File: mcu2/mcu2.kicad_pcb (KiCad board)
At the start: 2 copper layers, 96.7 x 58.3 mm, 36 parts, among them J1 KF128-5.08, J2 Conn_01x30, J8 Conn_01x30, Q1 WSF3085, Q2 PL4009, Q3 PL4009, U1 Pico, U2 motor_driver, U3 max31865_module, U4 dcdc_module

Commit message: mcu2 gerber
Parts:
- moved REF** 0.60 mm to (178.4, 141.5)
- moved REF** 0.51 mm to (178.3, 90.9)
- moved REF** 0.50 mm to (88.6, 141.5)
- moved REF** 0.44 mm to (88.6, 90.9)
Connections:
- J2 pad 6: GNDA -> THERM_AUX_2
- J2 pad 7: THERM_0 -> THERM_AUX_1
- J2 pad 8: THERM_AUX_1 -> THERM_0
- J2 pad 9: THERM_AUX_2 -> GNDA
- J8 pad 6: GNDA -> THERM_AUX_2
- J8 pad 7: THERM_0 -> THERM_AUX_1
- J8 pad 8: THERM_AUX_1 -> THERM_0
- J8 pad 9: THERM_AUX_2 -> GNDA
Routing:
- net +5V: track 28.0 -> 38.5 mm
- net GNDA: track 40.5 -> 33.0 mm, vias 0 -> 27
- net PROBE_ZMIN_24V: track 43.7 -> 37.7 mm
- net THERM_AUX_2: track 118.1 -> 112.7 mm, vias 2 -> 0
- net PART_FAN_CTRL: track 19.2 -> 13.9 mm
- net ADXL345_CS: track 49.6 -> 45.7 mm
- net ADXL345_SDO: track 53.4 -> 49.7 mm
- net SERVO_NEOPIXEL: track 61.9 -> 58.3 mm
- net GND: track 26.4 -> 29.5 mm, vias 19 -> 90
- net AUX2: track 28.6 -> 25.5 mm
- net E_DIR: track 42.5 -> 39.7 mm
- net STEPPER_A2: track 23.9 -> 21.6 mm
- net ADXL345_SDA: track 50.8 -> 48.7 mm
- net HEATER_CTRL: track 30.9 -> 28.9 mm
- net E_CS: track 45.4 -> 43.6 mm
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- added copper zone on B.Cu, net GND
- added copper zone on F.Cu, net GND
- added copper zone on F.Cu, net GNDA
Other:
- board size 96.7 x 58.3 mm -> 96.8 x 57.7 mm
- board text removed: "24V"
- board text removed: "3V3"
- board text removed: "CS"
- board text removed: "DIR"
- board text removed: "EN"
- board text removed: "G"
- board text removed: "GND"
- board text removed: "STEP"
- board text removed: "STEPPER"

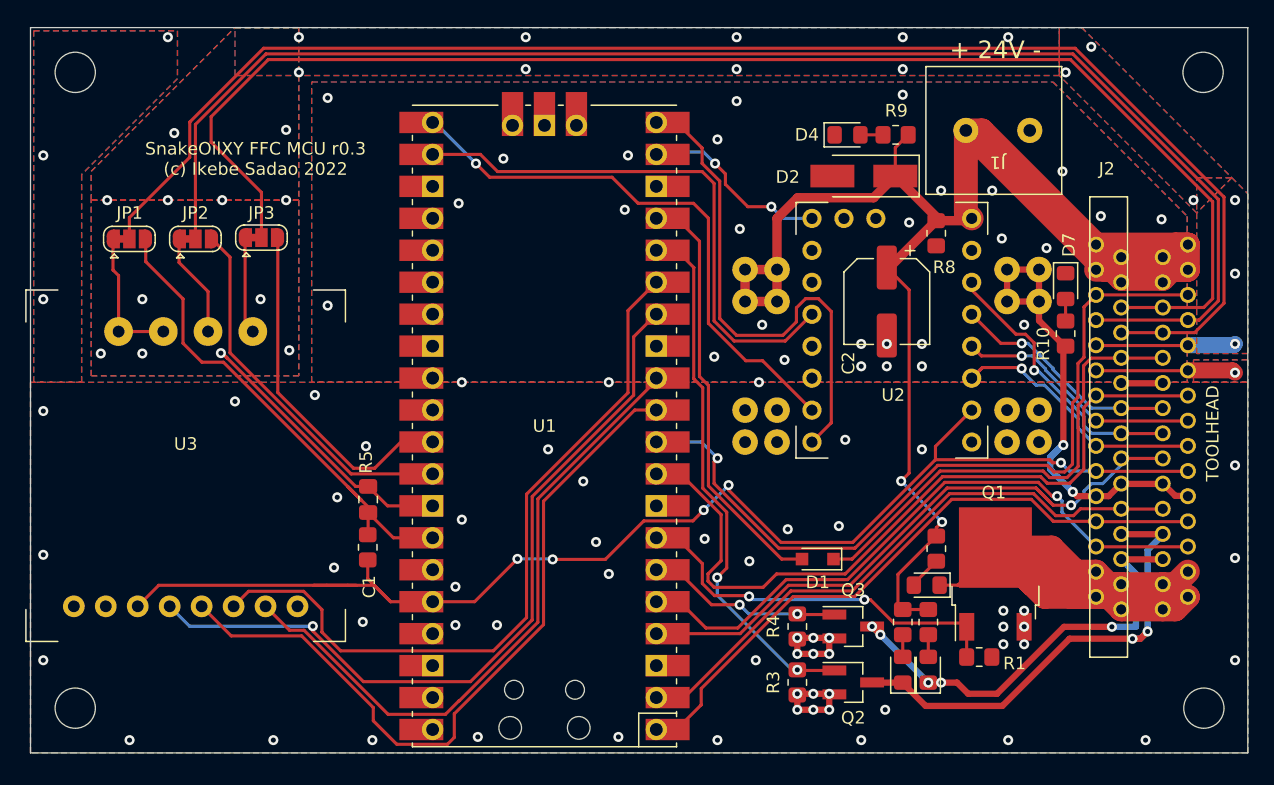
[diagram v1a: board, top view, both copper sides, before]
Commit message: change hole size
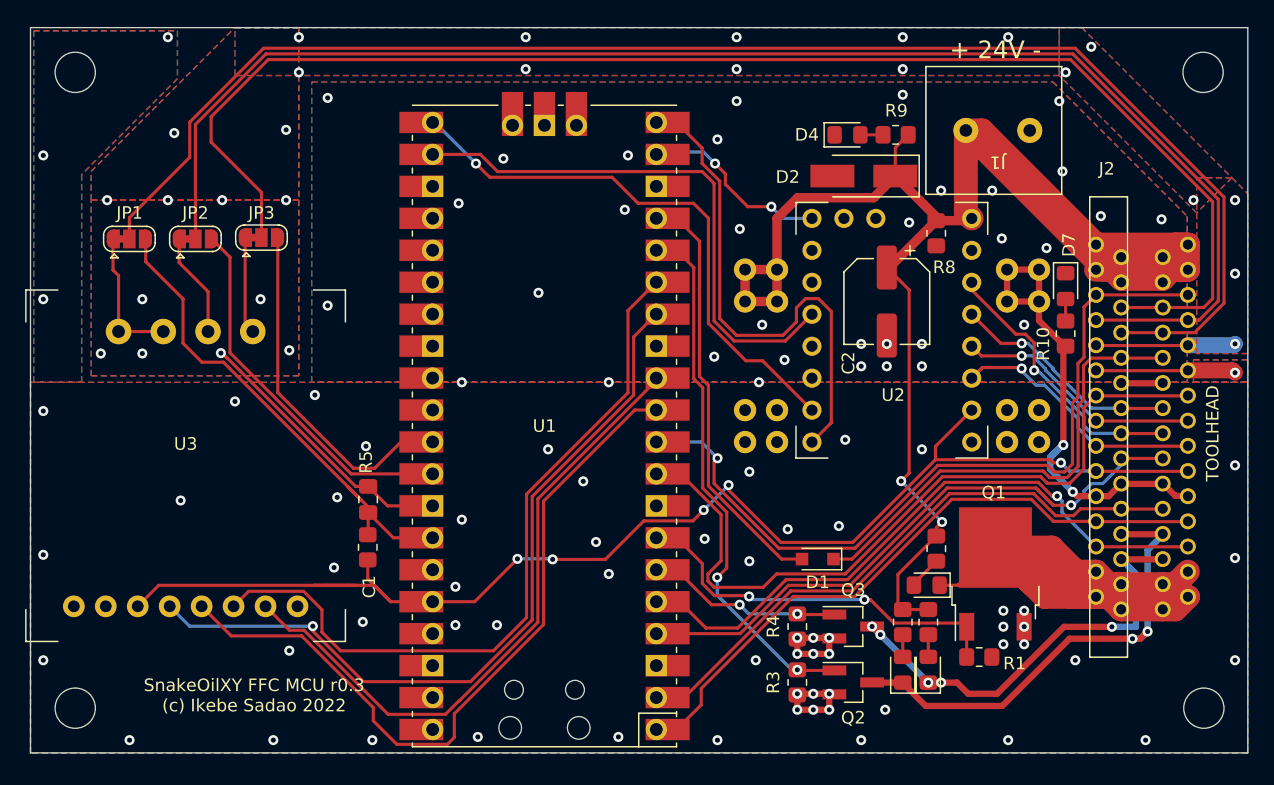
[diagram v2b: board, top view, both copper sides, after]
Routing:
- net GND: vias 90 -> 96

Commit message: r3 jlcpcb
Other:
- outline, holes or cut-outs redrawn
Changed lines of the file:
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@@
       (net 4 "HEATER_SW") (pinfunction "Pin_30") (pintype "passive"))
   )
-  (gr_rect (start 181.864 87.376) (end 85.09 145.034) (layer "Edge.Cuts") (width 0.1) (fill none))
+  (gr_line (start 180.594 145.034) (end 86.36 145.034) (layer "Edge.Cuts") (width 0.1))
+  (gr_line (start 85.09 143.764) (end 85.09 88.646) (layer "Edge.Cuts") (width 0.1))
+  (gr_arc (start 181.864 143.764) (mid 181.492026 144.662026) (end 180.594 145.034) (layer "Edge.Cuts") (width 0.1))
+  (gr_line (start 181.864 88.646) (end 181.864 143.764) (layer "Edge.Cuts") (width 0.1))
+  (gr_arc (start 86.36 145.034) (mid 85.461974 144.662026) (end 85.09 143.764) (layer "Edge.Cuts") (width 0.1))
+  (gr_arc (start 180.594 87.376) (mid 181.492026 87.747974) (end 181.864 88.646) (layer "Edge.Cuts") (width 0.1))
+  (gr_line (start 86.36 87.376) (end 180.594 87.376) (layer "Edge.Cuts") (width 0.1))
+  (gr_arc (start 85.09 88.646) (mid 85.461974 87.747974) (end 86.36 87.376) (layer "Edge.Cuts") (width 0.1))
   (gr_text "SnakeOilXY FFC MCU r0.3\n(c) Ikebe Sadao 2022" (at 102.87 140.462) (layer "F.SilkS")
     (effects (font (size 1 1) (thickness 0.15)))
